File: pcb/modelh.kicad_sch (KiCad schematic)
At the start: 46 parts, among them SW1 SW_Push, U1 GD32F103C8T6, U2 AMS1117-3.3, Y1 8MHz

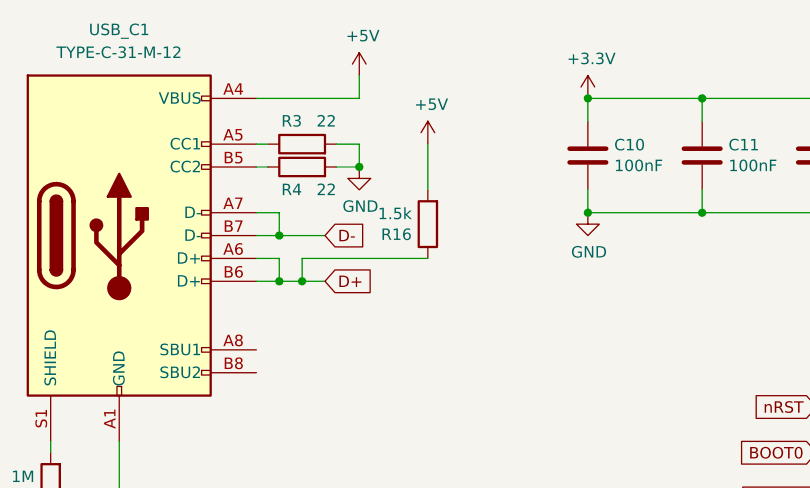
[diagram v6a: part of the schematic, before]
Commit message: Add proper CC resistors for USB C
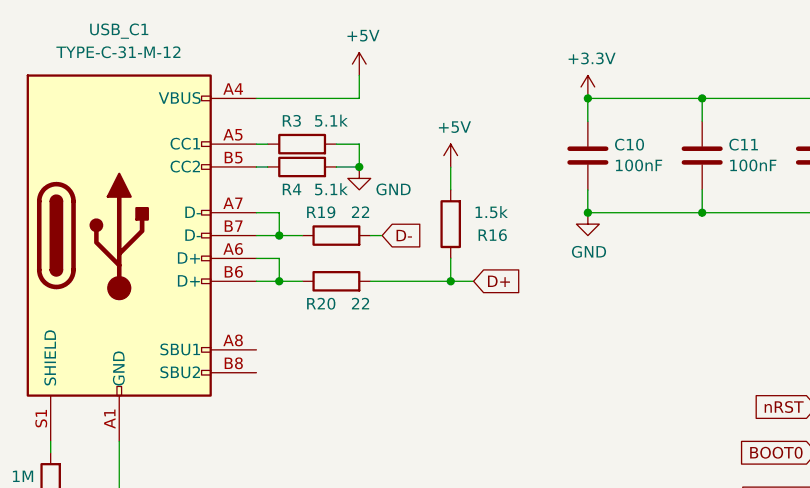
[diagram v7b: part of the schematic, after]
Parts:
- added R19, R20: 22, Resistor_SMD:R_0603_1608Metric, symbol Device:R
- R3, R4: value 22 -> 5.1k
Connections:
- net D+: now also R20.2; no longer USB_C1.A6 (D+), USB_C1.B6 (D+)
- net D-: now also R19.2; no longer USB_C1.A7 (D-), USB_C1.B7 (D-)
- new net: R20.1, USB_C1.A6 (D+), USB_C1.B6 (D+)
- new net: R19.1, USB_C1.A7 (D-), USB_C1.B7 (D-)
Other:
- moved on the sheet: R16
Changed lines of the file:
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@@
   (junction (at 121.92 39.37) (diameter 0) (color 0 0 0 0)
   )
-  (junction (at 64.77 46.99) (diameter 0) (color 0 0 0 0)
-  )
   (junction (at 180.34 43.18) (diameter 0) (color 0 0 0 0)
   )
@@
   )
   (junction (at 76.2 130.81) (diameter 0) (color 0 0 0 0)
+  )
+  (junction (at 81.28 46.99) (diameter 0) (color 0 0 0 0)
   )
   (junction (at 109.22 39.37) (diameter 0) (color 0 0 0 0)
@@
     (stroke (width 0) (type default) (color 0 0 0 0))
   )
-  (wire (pts (xy 64.77 46.99) (xy 67.31 46.99))
+  (wire (pts (xy 62.23 46.99) (xy 64.77 46.99))
     (stroke (width 0) (type default) (color 0 0 0 0))
   )
@@
     (stroke (width 0) (type default) (color 0 0 0 0))
   )
+  (wire (pts (xy 72.39 46.99) (xy 81.28 46.99))
+    (stroke (width 0) (type default) (color 0 0 0 0))
+  )
   (wire (pts (xy 124.46 73.66) (xy 129.54 73.66))
     (stroke (width 0) (type default) (color 0 0 0 0))
@@
     (stroke (width 0) (type default) (color 0 0 0 0))
   )
-  (wire (pts (xy 64.77 44.45) (xy 64.77 46.99))
-    (stroke (width 0) (type default) (color 0 0 0 0))
-  )
   (wire (pts (xy 72.39 88.9) (xy 83.82 88.9))
     (stroke (width 0) (type default) (color 0 0 0 0))
@@
     (stroke (width 0) (type default) (color 0 0 0 0))
   )
+  (wire (pts (xy 72.39 41.91) (xy 73.66 41.91))
+    (stroke (width 0) (type default) (color 0 0 0 0))
+  )
   (wire (pts (xy 162.56 121.92) (xy 170.18 121.92))
     (stroke (width 0) (type default) (color 0 0 0 0))
@@
     (stroke (width 0) (type default) (color 0 0 0 0))
   )
-  (wire (pts (xy 62.23 41.91) (xy 67.31 41.91))
+  (wire (pts (xy 62.23 41.91) (xy 64.77 41.91))
     (stroke (width 0) (type default) (color 0 0 0 0))
   )
@@
     (stroke (width 0) (type default) (color 0 0 0 0))
   )
+  (wire (pts (xy 81.28 46.99) (xy 83.82 46.99))
+    (stroke (width 0) (type default) (color 0 0 0 0))
+  )
   (wire (pts (xy 59.69 96.52) (xy 72.39 96.52))
     (stroke (width 0) (type default) (color 0 0 0 0))
@@
     (stroke (width 0) (type default) (color 0 0 0 0))
   )
-  (wire (pts (xy 78.74 31.75) (xy 78.74 36.83))
+  (wire (pts (xy 81.28 34.29) (xy 81.28 36.83))
     (stroke (width 0) (type default) (color 0 0 0 0))
   )
@@
     (stroke (width 0) (type default) (color 0 0 0 0))
   )
+  (wire (pts (xy 81.28 46.99) (xy 81.28 44.45))
+    (stroke (width 0) (type default) (color 0 0 0 0))
+  )
   (wire (pts (xy 248.92 99.06) (xy 255.27 99.06))
     (stroke (width 0) (type default) (color 0 0 0 0))
@@
   )
   (wire (pts (xy 269.24 146.05) (xy 266.7 146.05))
-    (stroke (width 0) (type default) (color 0 0 0 0))
-  )
-  (wire (pts (xy 62.23 46.99) (xy 64.77 46.99))
-    (stroke (width 0) (type default) (color 0 0 0 0))
-  )
-  (wire (pts (xy 78.74 44.45) (xy 64.77 44.45))
     (stroke (width 0) (type default) (color 0 0 0 0))
   )
@@
     )
   )
-  (global_label "D+" (shape input) (at 67.31 46.99 0) (fields_autoplaced)
+  (global_label "D+" (shape input) (at 83.82 46.99 0) (fields_autoplaced)
     (effects (font (size 1.27 1.27)) (justify left))
-    (property "Intersheet References" "${INTERSHEET_REFS}" (id 0) (at 2.54 13.97 0)
+    (property "Intersheet References" "${INTERSHEET_REFS}" (id 0) (at 19.05 13.97 0)
       (effects (font (size 1.27 1.27)) hide)
     )
@@
     )
   )
-  (global_label "D-" (shape input) (at 67.31 41.91 0) (fields_autoplaced)
+  (global_label "D-" (shape input) (at 73.66 41.91 0) (fields_autoplaced)
     (effects (font (size 1.27 1.27)) (justify left))
-    (property "Intersheet References" "${INTERSHEET_REFS}" (id 0) (at 2.54 6.35 0)
+    (property "Intersheet References" "${INTERSHEET_REFS}" (id 0) (at 8.89 6.35 0)
       (effects (font (size 1.27 1.27)) hide)
     )
@@
       (effects (font (size 1.27 1.27)) (justify left))
     )
-    (property "Value" "22" (id 1) (at 68.58 29.21 90)
+    (property "Value" "5.1k" (id 1) (at 69.85 29.21 90)
       (effects (font (size 1.27 1.27)) (justify left))
     )
@@
       (effects (font (size 1.27 1.27)) (justify left))
     )
-    (property "Value" "22" (id 1) (at 68.58 36.83 90)
+    (property "Value" "5.1k" (id 1) (at 69.85 36.83 90)
       (effects (font (size 1.27 1.27)) (justify left))
     )
@@
       (effects (font (size 1.27 1.27)) hide)
     )
-    (property "Value" "GND" (id 1) (at 71.247 38.6842 0))
+    (property "Value" "GND" (id 1) (at 74.93 36.83 0))
     (property "Footprint" "" (id 2) (at 71.12 34.29 0)
       (effects (font (size 1.27 1.27)) hide)
@@
     (pin "4")
   )
-  (symbol (lib_id "power:+5V") (at 78.74 31.75 0) (unit 1)
-    (in_bom yes) (on_board yes)
-    (property "Reference" "#PWR0127" (id 0) (at 78.74 35.56 0)
-      (effects (font (size 1.27 1.27)) hide)
-    )
-    (property "Value" "+5V" (id 1) (at 79.121 27.3558 0))
-    (property "Footprint" "" (id 2) (at 78.74 31.75 0)
-      (effects (font (size 1.27 1.27)) hide)
-    )
-    (property "Datasheet" "" (id 3) (at 78.74 31.75 0)
-      (effects (font (size 1.27 1.27)) hide)
-    )
-    (pin "1")
+  (symbol (lib_id "Device:R") (at 68.58 46.99 90) (unit 1)
+    (in_bom yes) (on_board yes)
+    (property "Reference" "R20" (id 0) (at 68.58 49.53 90)
+      (effects (font (size 1.27 1.27)) (justify left))
+    )
+    (property "Value" "22" (id 1) (at 72.39 49.53 90)
+      (effects (font (size 1.27 1.27)) (justify left))
+    )
+    (property "Footprint" "Resistor_SMD:R_0603_1608Metric" (id 2) (at 68.58 48.768 90)
+      (effects (font (size 1.27 1.27)) hide)
+    )
+    (property "Datasheet" "~" (id 3) (at 68.58 46.99 0)
+      (effects (font (size 1.27 1.27)) hide)
+    )
+    (property "LCSC" "C23345" (id 4) (at 68.58 46.99 0)
+      (effects (font (size 1.27 1.27)) hide)
+    )
+    (pin "1")
+    (pin "2")
+  )
+  (symbol (lib_id "power:+5V") (at 81.28 34.29 0) (unit 1)
+    (in_bom yes) (on_board yes)
+    (property "Reference" "#PWR0127" (id 0) (at 81.28 38.1 0)
+      (effects (font (size 1.27 1.27)) hide)
+    )
+    (property "Value" "+5V" (id 1) (at 81.661 29.8958 0))
+    (property "Footprint" "" (id 2) (at 81.28 34.29 0)
+      (effects (font (size 1.27 1.27)) hide)
+    )
+    (property "Datasheet" "" (id 3) (at 81.28 34.29 0)
+      (effects (font (size 1.27 1.27)) hide)
+    )
+    (pin "1")
+  )
+  (symbol (lib_id "Device:R") (at 68.58 41.91 90) (unit 1)
+    (in_bom yes) (on_board yes)
+    (property "Reference" "R19" (id 0) (at 68.58 39.37 90)
+      (effects (font (size 1.27 1.27)) (justify left))
+    )
+    (property "Value" "22" (id 1) (at 72.39 39.37 90)
+      (effects (font (size 1.27 1.27)) (justify left))
+    )
+    (property "Footprint" "Resistor_SMD:R_0603_1608Metric" (id 2) (at 68.58 43.688 90)
+      (effects (font (size 1.27 1.27)) hide)
+    )
+    (property "Datasheet" "~" (id 3) (at 68.58 41.91 0)
+      (effects (font (size 1.27 1.27)) hide)
+    )
+    (property "LCSC" "C23345" (id 4) (at 68.58 41.91 0)
+      (effects (font (size 1.27 1.27)) hide)
+    )
+    (pin "1")
+    (pin "2")
   )
   (symbol (lib_id "Connector:USB_C_Receptacle_USB2.0") (at 44.45 41.91 0) (unit 1)
@@
     (pin "S1")
   )
-  (symbol (lib_id "Device:R") (at 78.74 40.64 180) (unit 1)
-    (in_bom yes) (on_board yes)
-    (property "Reference" "R16" (id 0) (at 76.962 41.8084 0)
-      (effects (font (size 1.27 1.27)) (justify left))
-    )
-    (property "Value" "1.5k" (id 1) (at 76.962 39.497 0)
-      (effects (font (size 1.27 1.27)) (justify left))
-    )
-    (property "Footprint" "Resistor_SMD:R_0603_1608Metric" (id 2) (at 80.518 40.64 90)
-      (effects (font (size 1.27 1.27)) hide)
-    )
-    (property "Datasheet" "~" (id 3) (at 78.74 40.64 0)
-      (effects (font (size 1.27 1.27)) hide)
-    )
-    (property "LCSC" "C22843" (id 4) (at 78.74 40.64 0)
+  (symbol (lib_id "Device:R") (at 81.28 40.64 180) (unit 1)
+    (in_bom yes) (on_board yes)
+    (property "Reference" "R16" (id 0) (at 87.63 41.91 0)
+      (effects (font (size 1.27 1.27)) (justify left))
+    )
+    (property "Value" "1.5k" (id 1) (at 87.63 39.37 0)
+      (effects (font (size 1.27 1.27)) (justify left))
+    )
+    (property "Footprint" "Resistor_SMD:R_0603_1608Metric" (id 2) (at 83.058 40.64 90)
+      (effects (font (size 1.27 1.27)) hide)
+    )
+    (property "Datasheet" "~" (id 3) (at 81.28 40.64 0)
+      (effects (font (size 1.27 1.27)) hide)
+    )
+    (property "LCSC" "C22843" (id 4) (at 81.28 40.64 0)
       (effects (font (size 1.27 1.27)) hide)
     )
@@
     )
     (path "/00000000-0000-0000-0000-00005edacaa8"
-      (reference "R3") (unit 1) (value "22") (footprint "Resistor_SMD:R_0603_1608Metric")
+      (reference "R3") (unit 1) (value "5.1k") (footprint "Resistor_SMD:R_0603_1608Metric")
     )
     (path "/00000000-0000-0000-0000-00005edc1f8e"
-      (reference "R4") (unit 1) (value "22") (footprint "Resistor_SMD:R_0603_1608Metric")
+      (reference "R4") (unit 1) (value "5.1k") (footprint "Resistor_SMD:R_0603_1608Metric")
     )
     (path "/00000000-0000-0000-0000-00005f44a2ec"
@@
       (reference "R18") (unit 1) (value "100k") (footprint "Resistor_SMD:R_0603_1608Metric")
     )
+    (path "/5dbffd9b-898c-4196-85a1-1ee3ece1857c"
+      (reference "R19") (unit 1) (value "22") (footprint "Resistor_SMD:R_0603_1608Metric")
+    )
+    (path "/21672ee7-aad2-4671-b0fe-0e977acd45d5"
+      (reference "R20") (unit 1) (value "22") (footprint "Resistor_SMD:R_0603_1608Metric")
+    )
     (path "/0e11df2a-9272-4499-afc2-aedc65005ea5"

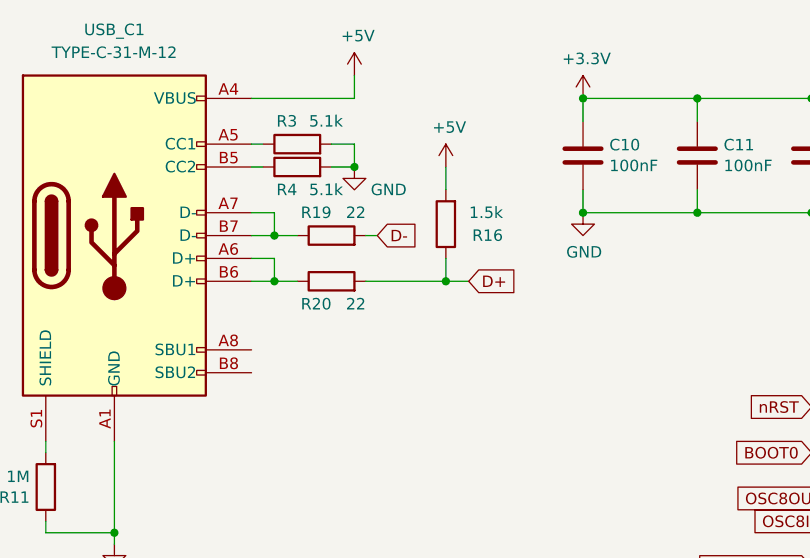
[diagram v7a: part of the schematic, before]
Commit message: Move pull up in front of 0 ohm resistors
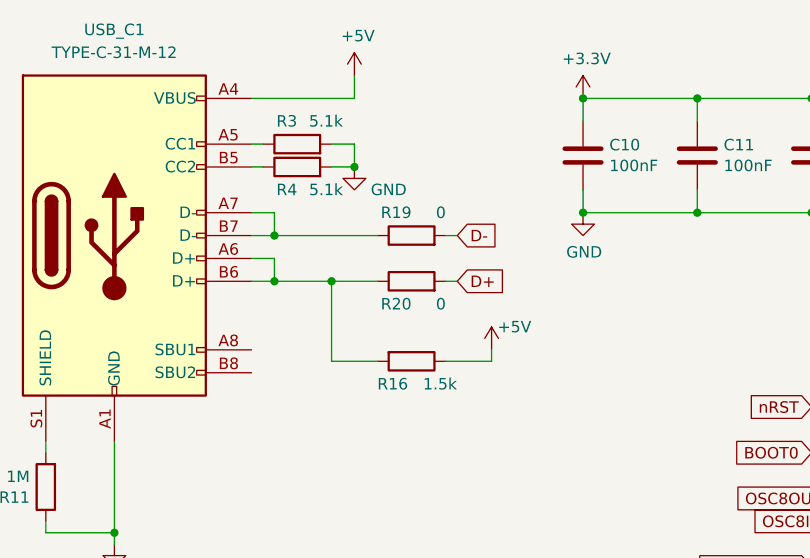
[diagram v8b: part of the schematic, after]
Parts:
- R19, R20: value 22 -> 0
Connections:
- net +5V: now also R16.1; no longer R16.2
- net D+: no longer R16.1
- net at R20.1, USB_C1.A6 (D+), USB_C1.B6 (D+): now also R16.2
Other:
- moved on the sheet: R16, R19, R20
